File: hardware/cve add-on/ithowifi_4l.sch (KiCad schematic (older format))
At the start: 32 parts, among them J1 CONN_01X07, J2 conn, J3 Conn_Coaxial, J4 TC2030-MCP-NL, J5 Conn_02x02_Odd_Even, Q1 BSS138, Q2 BSS138, SW1 Fail safe, SW2 Reset, U1 ESP32-WROOM, U2 CC1101-868MHz-Module

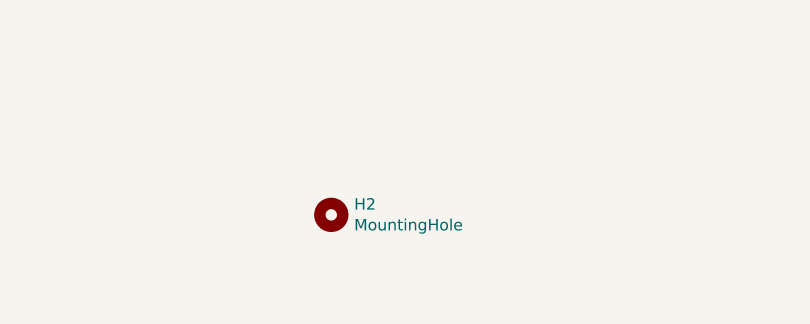
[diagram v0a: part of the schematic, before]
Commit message: Version 2.3-beta5
- fix: prevent crashes unsupported or partly supported itho devices
- breaking: On the up-side; all settings and labels have been regenerated and checked (and some translated) with a script, units have been added where available and labels are more descriptive. On the flip-side; automations based on the API, specifically the itho status label based automations might need to be updated.
- add: support for itho HeatPumt (WPU) devices and AutoTemp devices.

Please check labels for status and settings, if you see anything wrong, please let me know.
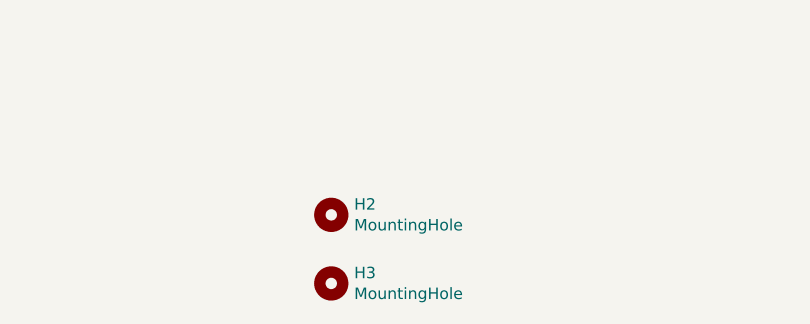
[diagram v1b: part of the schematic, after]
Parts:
- added H3: MountingHole, MountingHole:MountingHole_2.5mm, symbol Mechanical:MountingHole
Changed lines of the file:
@@
 Wire Wire Line
 	10875 6900 10950 6900
+$Comp
+L Mechanical:MountingHole H3
+U 1 1 61941A13
+P 10300 10575
+F 0 "H3" H 10400 10621 50  0000 L CNN
+F 1 "MountingHole" H 10400 10530 50  0000 L CNN
+F 2 "MountingHole:MountingHole_2.5mm" H 10300 10575 50  0001 C CNN
+F 3 "~" H 10300 10575 50  0001 C CNN
+	1    10300 10575
+	1    0    0    -1
+$EndComp
 $EndSCHEMATC
